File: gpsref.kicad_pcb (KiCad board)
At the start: 4 copper layers, 79.8 x 47.2 mm, 156 parts, among them J10 Skedd, J13 Boot, J2 SMA, J3 SMA, J4 SMA, J5 U.Fl, J6 SMA, J7 USB_C_Receptacle_16P, J8 U.Fl, J9 U.Fl, Q1 AO3400A, Q2 AO3401A, T2 MABA-010247-2R1250, U1 MAX-M10S, U11 74LVC1G07, U2 LMK05318BRGZR, U21 TMP117xxDRV, U3 TG5032CGN, U31 TLV3601DCKR, U32 TLV3601DCKR, U4 STM32H503KBUx, U5 TPS82084SIL, U6 TPS82084SIL, U7 TPS7A8801RTJR

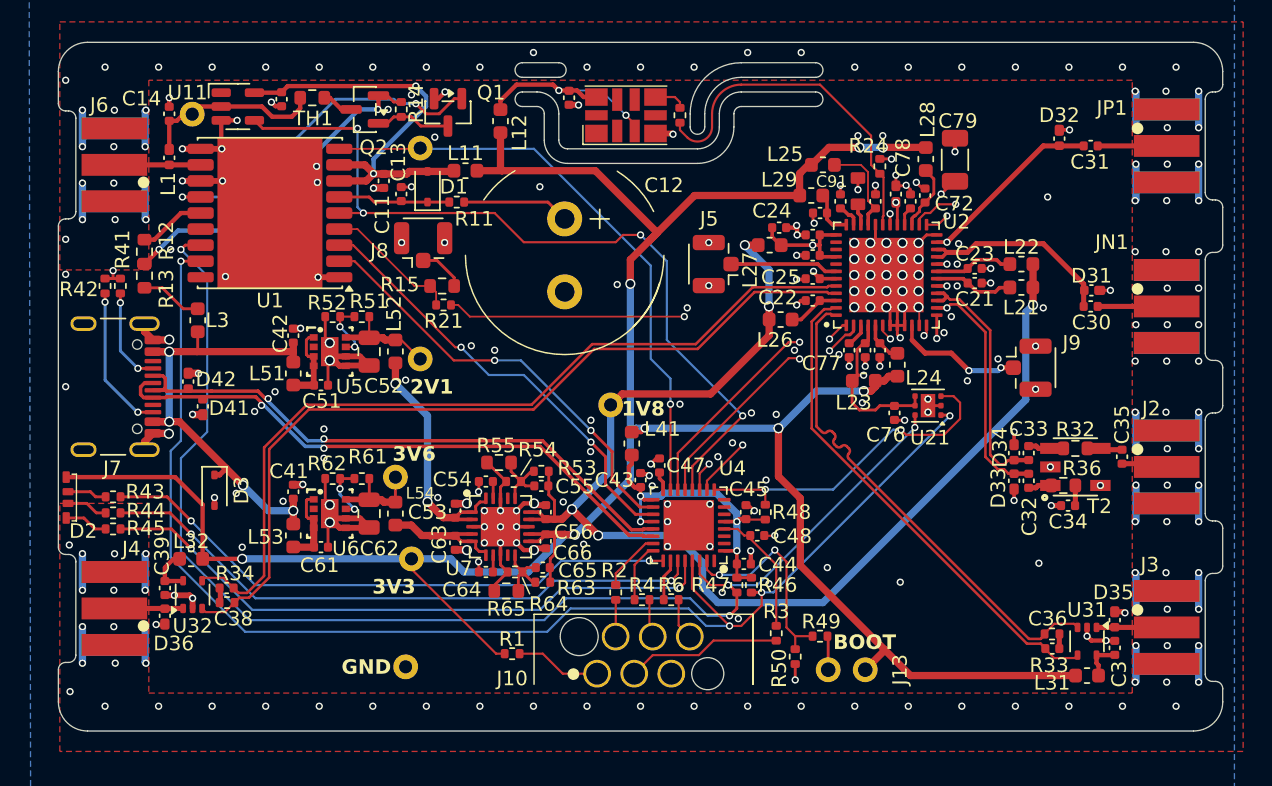
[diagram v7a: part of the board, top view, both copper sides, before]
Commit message: Add bias resistors to comparators.
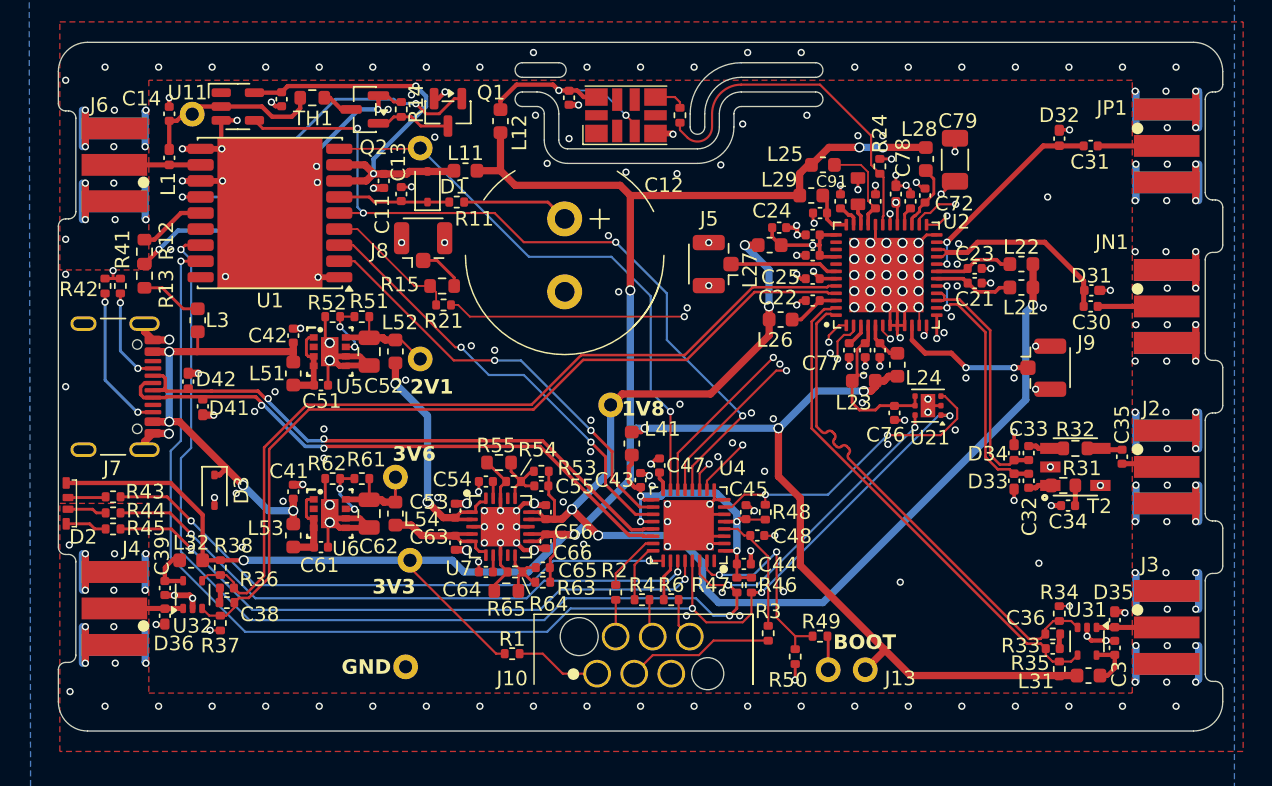
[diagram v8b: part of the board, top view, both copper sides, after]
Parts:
- added R34: 100k, Resistor_SMD:R_0402_1005Metric, F.Cu at (167.4, 115.5)
- added R35: 100k, Resistor_SMD:R_0402_1005Metric, F.Cu at (167.4, 119.3)
- added R37: 100k, Resistor_SMD:R_0402_1005Metric, F.Cu at (109.9, 116.2)
- added R38: 100k, Resistor_SMD:R_0402_1005Metric, F.Cu at (109.9, 112.4)
- moved J9 1.00 mm to (166.3, 98.7)
- moved R3 0.55 mm to (147.4, 116.9)
- moved D2 0.40 mm to (99.3, 108.0)
- moved TP7 0.14 mm to (122.9, 111.9)
- moved L32 0.10 mm to (107.9, 111.9)
- moved L31 0.10 mm to (169.4, 119.8)
- renumbered R36 to R31, R34 to R36
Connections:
- U4 pad 2: unconnected-(U4-PC14-Pad2) -> GND
- U4 pad 3: unconnected-(U4-PC15-Pad3) -> GND
- U4 pad 6: unconnected-(U4-PA0-Pad6) -> GND
- U4 pad 7: unconnected-(U4-PA1-Pad7) -> ALERT
- U4 pad 8: unconnected-(U4-PA2-Pad8) -> GND
- U4 pad 9: ALERT -> GND
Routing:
- net GND: track 166.4 -> 199.5 mm, vias 290 -> 302
- net I2C_SCL: track 112.3 -> 109.5 mm
- net ALERT: track 22.8 -> 21.0 mm
- net EXTINT: track 56.7 -> 55.0 mm
- net +3V3: track 174.7 -> 173.2 mm
- net GPS_nRST: track 40.5 -> 39.3 mm
- net I2C_SDA: track 108.4 -> 107.5 mm
- net /Clocking/SecRef: track 8.90 -> 9.74 mm
- net Net-(U31-V+): track 2.69 -> 3.39 mm
- net FDEC: track 17.6 -> 18.3 mm
- net OUT5: track 8.04 -> 7.40 mm
- net /CPU/dRST: track 10.7 -> 10.1 mm
